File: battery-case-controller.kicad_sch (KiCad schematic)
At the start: 22 parts

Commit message: finished schematics
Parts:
- removed U?: Housing, footprints:RND-455-00370, symbol Mechanical:Housing_Pad
- J21, J22: renamed from U?; LCSC# (none) -> C157923
- J27, J28, J29, J30, J31: renamed from U?; footprint footprints:8X8X8.4MM TERMINAL -> MountingHole:MountingHole_2.2mm_M2_Pad_Via
- gave numbers to parts that had none: 14
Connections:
- net phase_a/VREF is gone; now on net Interface/VREF: R21.1
- net mcu/AIN_VDC: now reaches C22.1, R23.2, R24.1
- net mcu/AIN_TEMP: now reaches C21.1, R21.2, R22.1
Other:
- sheet mcu ports: added AIN_IA, AIN_IB, AIN_IC, AIN_TEMP, AIN_VA, AIN_VB, AIN_VC, AIN_VDC, PWM_A, PWM_AN, PWM_B, PWM_BN, PWM_C, PWM_CN, VREF; removed none
- sheet phase_a ports: added V; removed none
- sheet phase_b ports: added V; removed none
- sheet phase_c ports: added V; removed none
- company: (none) -> UNIMOC universal motor controller
- title: (none) -> (BCC) Battery Case Controller

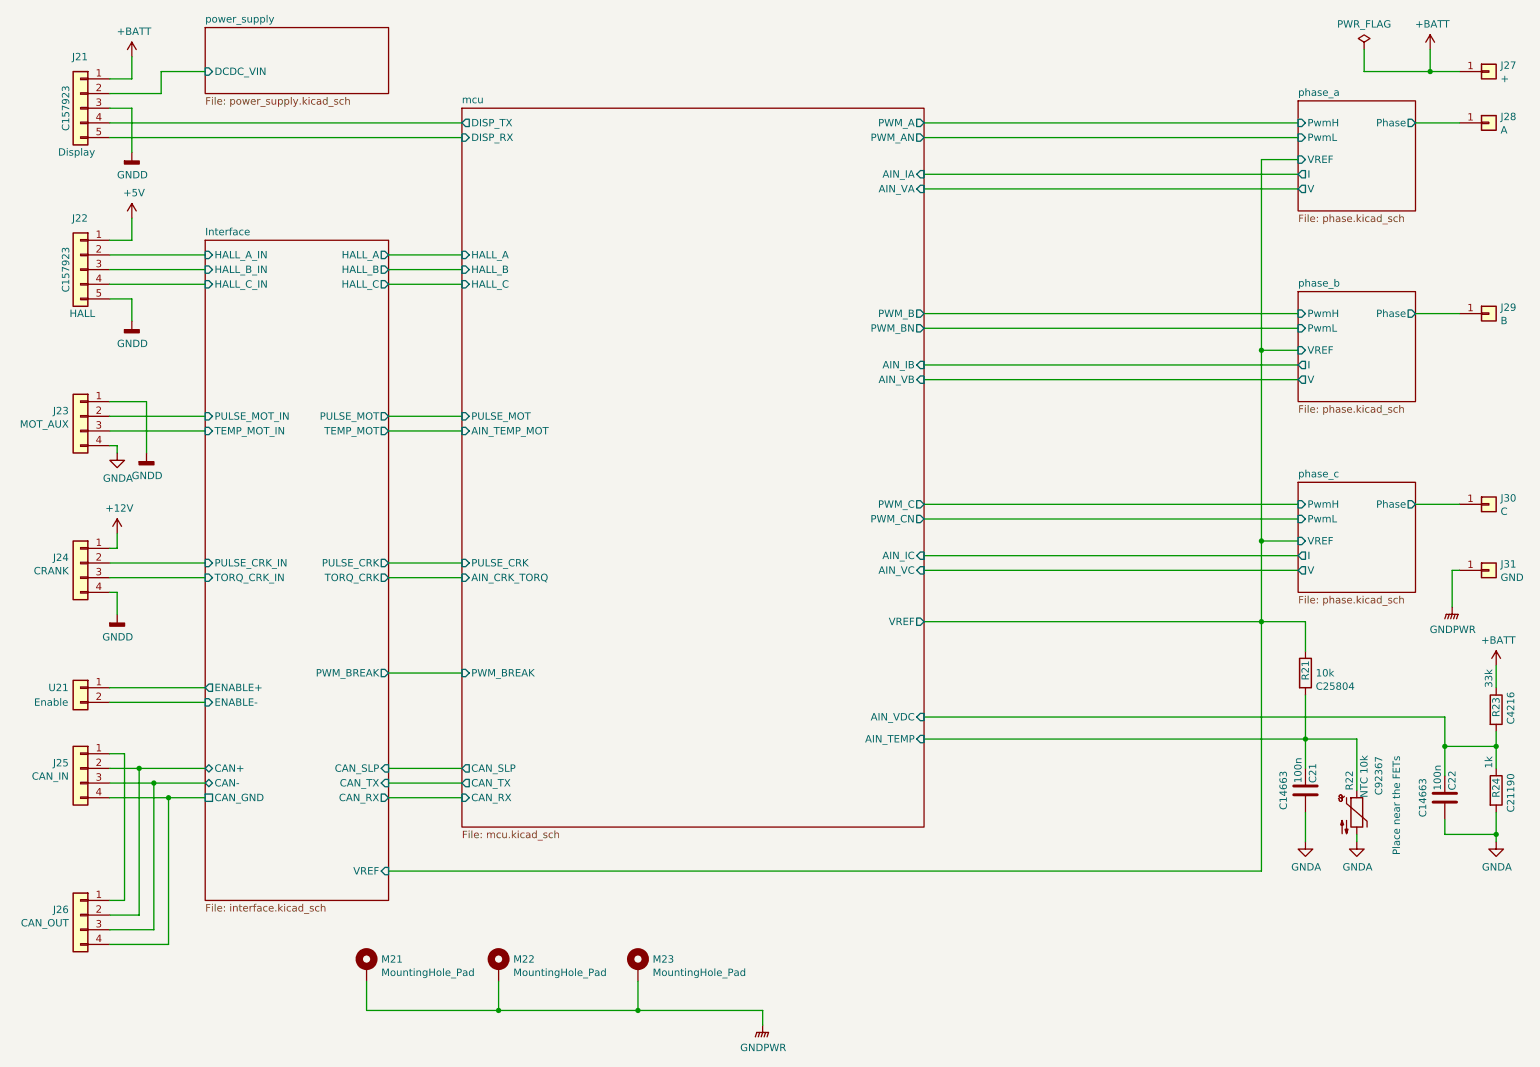
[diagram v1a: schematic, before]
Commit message: Placing first round finished
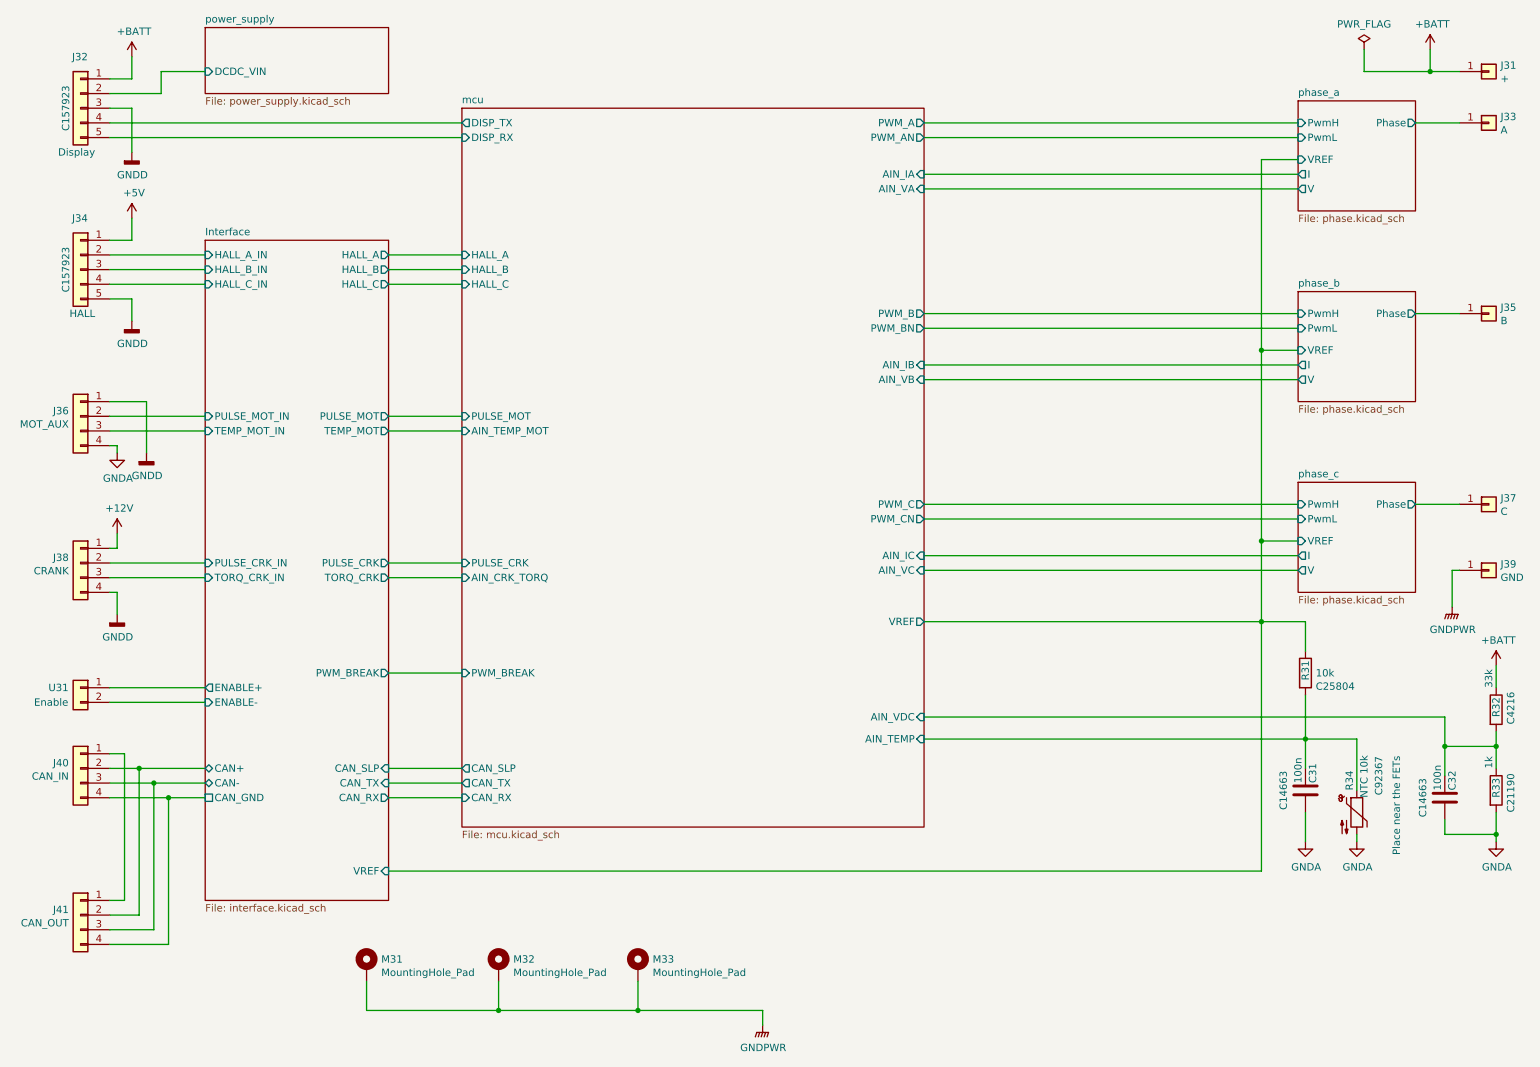
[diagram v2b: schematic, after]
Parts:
- renumbered C21 to C31, C22 to C32, J27 to J31, J21 to J32, J28 to J33, J22 to J34, J29 to J35, J23 to J36, J30 to J37, J24 to J38, J31 to J39, J25 to J40, J26 to J41, M21 to M31, M22 to M32, M23 to M33, R21 to R31, R23 to R32, R24 to R33, R22 to R34, U21 to U31
